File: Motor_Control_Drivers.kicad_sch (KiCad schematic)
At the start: 0 parts

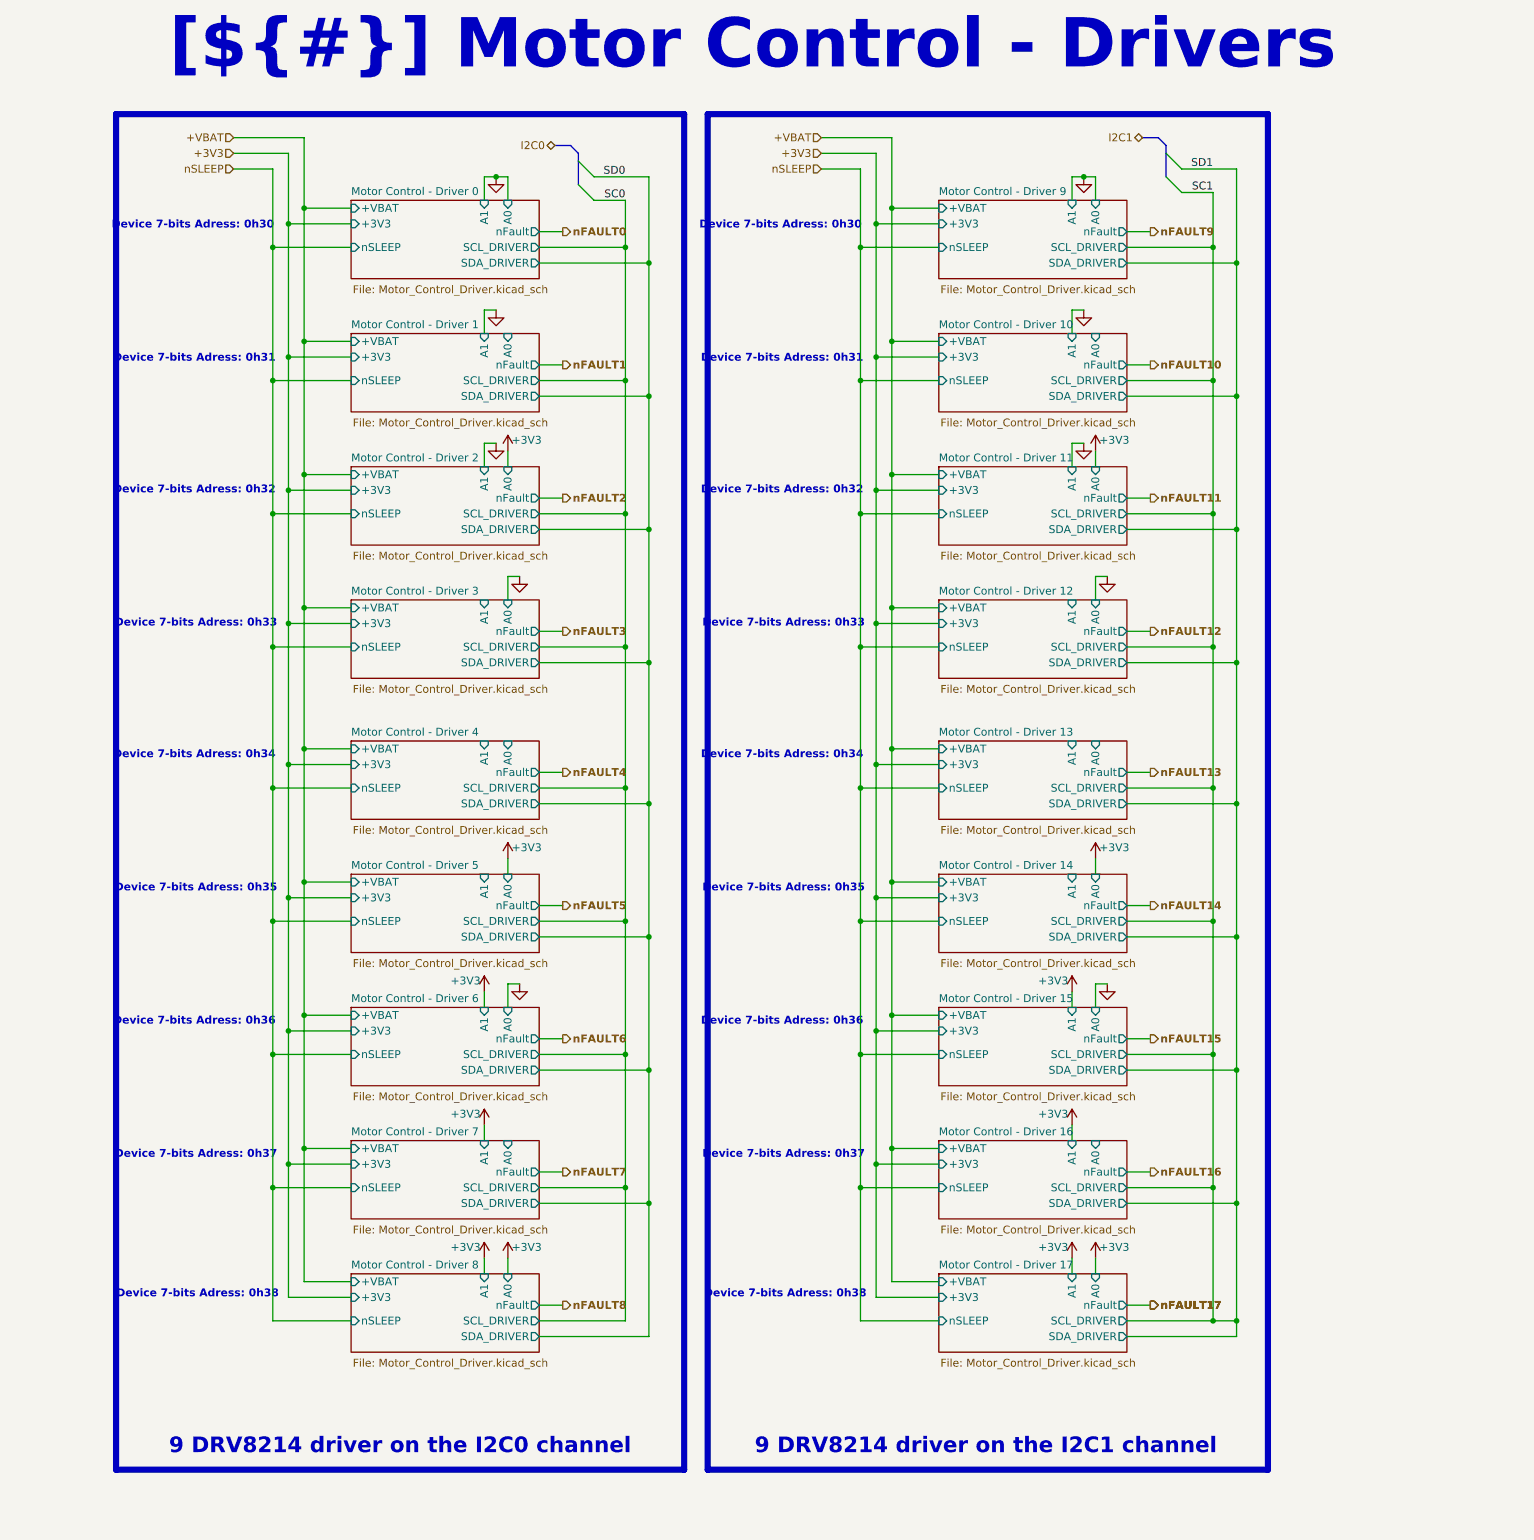
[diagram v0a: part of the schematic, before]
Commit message: Added footprints, images, almost finished all èages except for the MCU
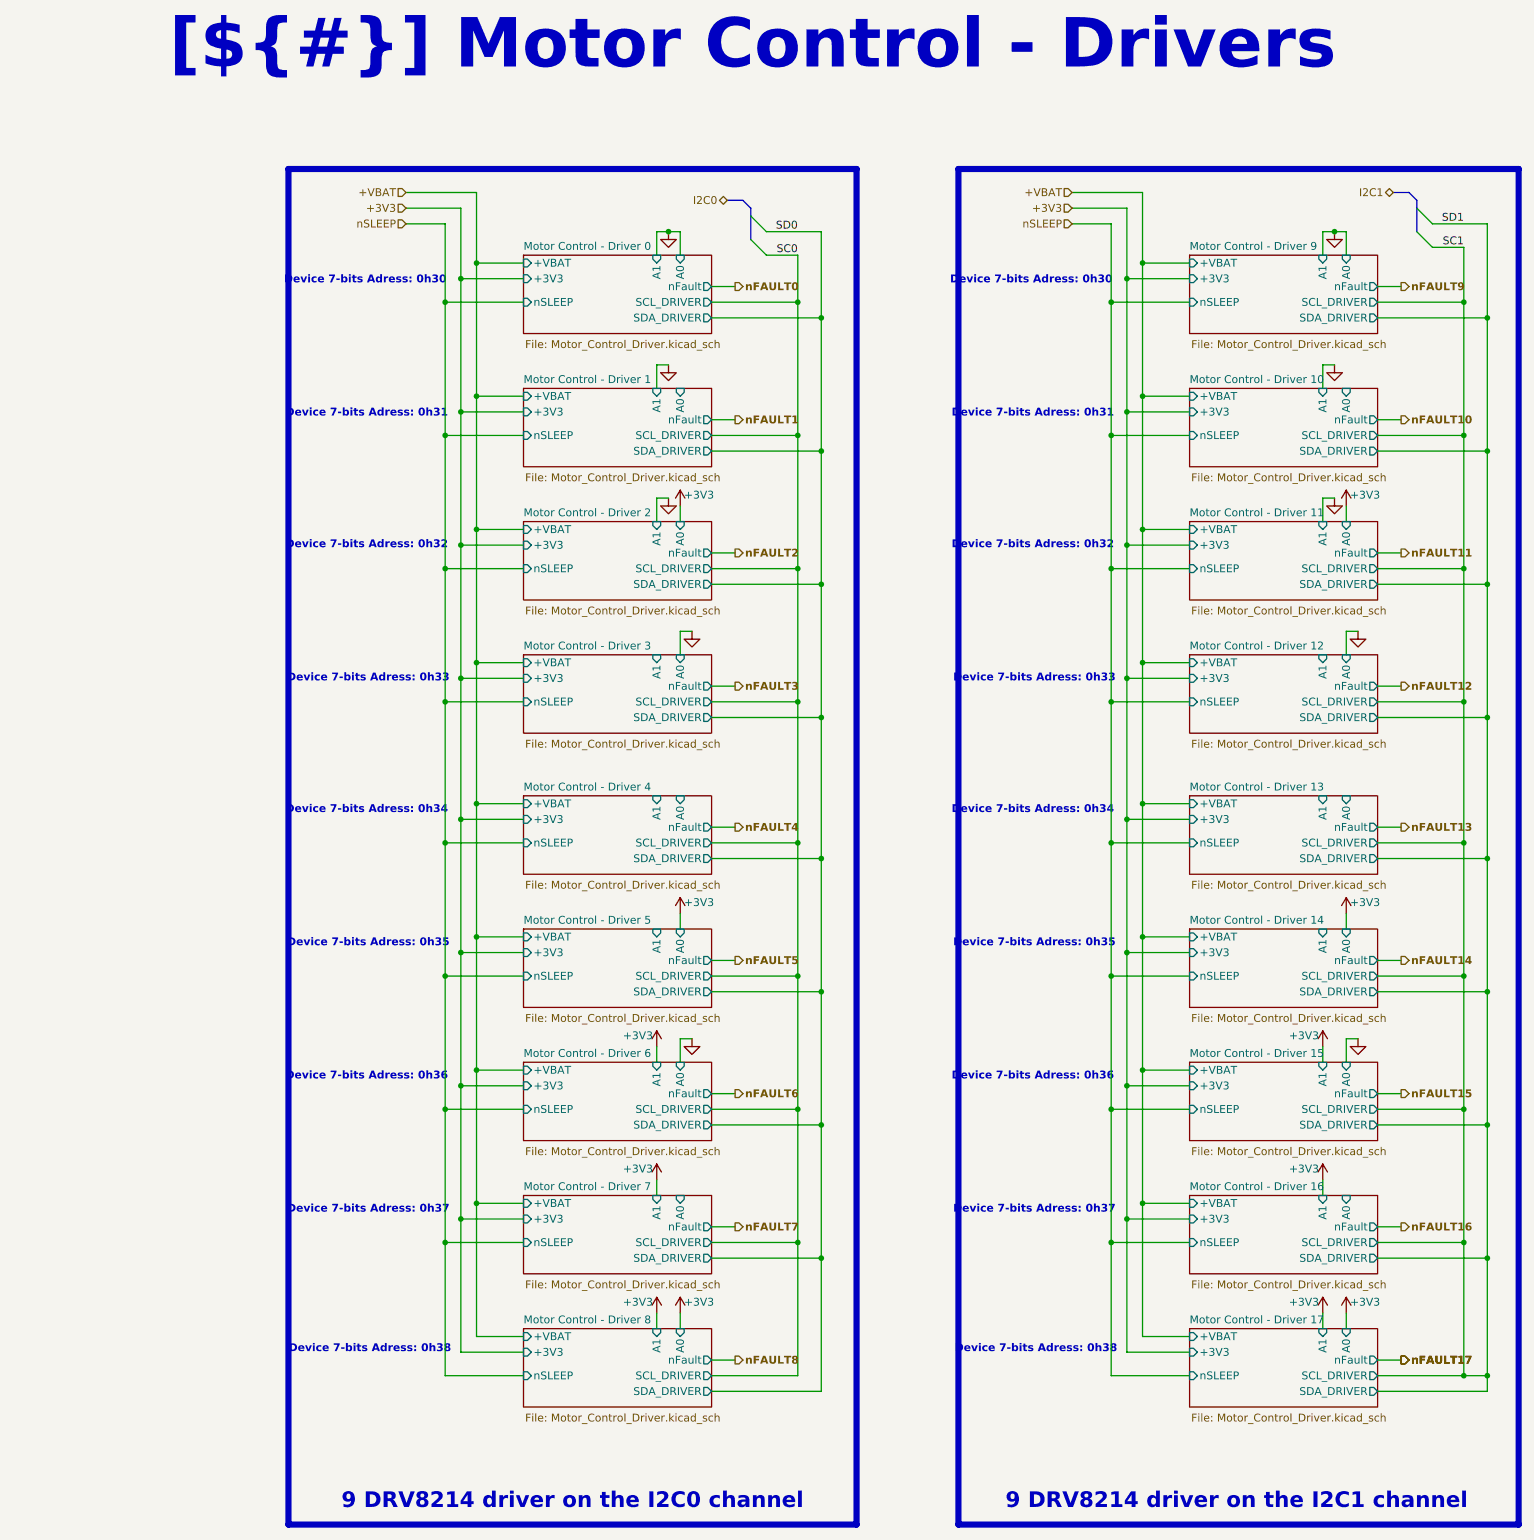
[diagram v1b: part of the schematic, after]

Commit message: Added RGB LED, added motor connectors, added test points, imported all 3D models
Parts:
- added J902: SEI-115-02-G-S-M-AB or SEI-115-02-GF-S-M-AB, symbol Connector_Generic:Conn_01x15
- added J903: SEI-125-02-G-S-E-AB est dispo, symbol Connector_Generic:Conn_01x25
- added TP901: nSLEEP_FRONT, 0_Plume:TestPoint_Pad_D0.5mm_Back, symbol Connector:TestPoint
- added TP902: nSLEEP_REAR, 0_Plume:TestPoint_Pad_D0.5mm_Back, symbol Connector:TestPoint
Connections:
- new net Motor Control - Driver 0/OUT1: J903.2 (Pin_2)
- new net Motor Control - Driver 0/OUT2: J903.3 (Pin_3)
- new net Motor Control - Driver 1/OUT1: J903.4 (Pin_4)
- new net Motor Control - Driver 1/OUT2: J903.5 (Pin_5)
- new net Motor Control - Driver 10/OUT1: J902.1 (Pin_1)
- new net Motor Control - Driver 10/OUT2: J902.2 (Pin_2)
- new net Motor Control - Driver 11/OUT1: J903.23 (Pin_23)
- new net Motor Control - Driver 11/OUT2: J903.24 (Pin_24)
- new net Motor Control - Driver 12/OUT1: J902.3 (Pin_3)
- new net Motor Control - Driver 12/OUT2: J902.4 (Pin_4)
- new net Motor Control - Driver 13/OUT1: J902.5 (Pin_5)
- new net Motor Control - Driver 13/OUT2: J902.6 (Pin_6)
- new net Motor Control - Driver 14/OUT1: J902.8 (Pin_8)
- new net Motor Control - Driver 14/OUT2: J902.9 (Pin_9)
- new net Motor Control - Driver 15/OUT1: J902.10 (Pin_10)
- new net Motor Control - Driver 15/OUT2: J902.11 (Pin_11)
- new net Motor Control - Driver 16/OUT1: J902.12 (Pin_12)
- new net Motor Control - Driver 16/OUT2: J902.13 (Pin_13)
- new net Motor Control - Driver 17/OUT1: J902.14 (Pin_14)
- new net Motor Control - Driver 17/OUT2: J902.15 (Pin_15)
- new net Motor Control - Driver 2/OUT1: J903.6 (Pin_6)
- new net Motor Control - Driver 2/OUT2: J903.7 (Pin_7)
- new net Motor Control - Driver 3/OUT1: J903.8 (Pin_8)
- new net Motor Control - Driver 3/OUT2: J903.9 (Pin_9)
- new net Motor Control - Driver 4/OUT1: J903.10 (Pin_10)
- new net Motor Control - Driver 4/OUT2: J903.11 (Pin_11)
- new net Motor Control - Driver 5/OUT1: J903.12 (Pin_12)
- new net Motor Control - Driver 5/OUT2: J903.14 (Pin_14)
- new net Motor Control - Driver 6/OUT1: J903.15 (Pin_15)
- new net Motor Control - Driver 6/OUT2: J903.16 (Pin_16)
- new net Motor Control - Driver 7/OUT1: J903.17 (Pin_17)
- new net Motor Control - Driver 7/OUT2: J903.18 (Pin_18)
- new net Motor Control - Driver 8/OUT1: J903.19 (Pin_19)
- new net Motor Control - Driver 8/OUT2: J903.20 (Pin_20)
- new net Motor Control - Driver 9/OUT1: J903.21 (Pin_21)
- new net Motor Control - Driver 9/OUT2: J903.22 (Pin_22)
- new net nSLEEP_FRONT: TP901.1
- new net nSLEEP_REAR: TP902.1
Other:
- sheet Motor Control - Driver 0 ports: added OUT1, OUT2; removed none
- sheet Motor Control - Driver 1 ports: added OUT1, OUT2; removed none
- sheet Motor Control - Driver 10 ports: added OUT1, OUT2; removed none
- sheet Motor Control - Driver 11 ports: added OUT1, OUT2; removed none
- sheet Motor Control - Driver 12 ports: added OUT1, OUT2; removed none
- sheet Motor Control - Driver 13 ports: added OUT1, OUT2; removed none
- sheet Motor Control - Driver 14 ports: added OUT1, OUT2; removed none
- sheet Motor Control - Driver 15 ports: added OUT1, OUT2; removed none
- sheet Motor Control - Driver 16 ports: added OUT1, OUT2; removed none
- sheet Motor Control - Driver 17 ports: added OUT1, OUT2; removed none
- sheet Motor Control - Driver 2 ports: added OUT1, OUT2; removed none
- sheet Motor Control - Driver 3 ports: added OUT1, OUT2; removed none
- sheet Motor Control - Driver 4 ports: added OUT1, OUT2; removed none
- sheet Motor Control - Driver 5 ports: added OUT1, OUT2; removed none
- sheet Motor Control - Driver 6 ports: added OUT1, OUT2; removed none
- sheet Motor Control - Driver 7 ports: added OUT1, OUT2; removed none
- sheet Motor Control - Driver 8 ports: added OUT1, OUT2; removed none
- sheet Motor Control - Driver 9 ports: added OUT1, OUT2; removed none

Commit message: Finished schematic, imported all footprints, all 3D models and created STM32 project, now need to proofread shematic before layout
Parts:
- J901: renamed from J903; value SEI-125-02-G-S-E-AB est dispo -> SEI-125-02-GF-S-M-AT; footprint (none) -> 0_Plume:SAMTEC_SEI-125-02-GF-S-M-AT; Manufacturer (none) -> Samtec; Manufacturer Part Number (none) -> SEI-125-02-GF-S-M-AT; Supplier (none) -> Samtec; Supplier Part Number (none) -> SEI-125-02-GF-S-M-AT; now left out of the parts list
- J902: value SEI-115-02-G-S-M-AB or SEI-115-02-GF-S-M-AB -> SEI-115-02-GF-S-M-AT; footprint (none) -> 0_Plume:SAMTEC_SEI-115-02-GF-S-M-AT; Manufacturer (none) -> Samtec; Manufacturer Part Number (none) -> SEI-115-02-GF-S-M-AT; Supplier (none) -> Samtec; Supplier Part Number (none) -> SEI-115-02-GF-S-M-AT; now left out of the parts list
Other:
- moved on the sheet: TP901, TP902
